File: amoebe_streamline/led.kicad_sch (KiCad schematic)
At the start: 1 part

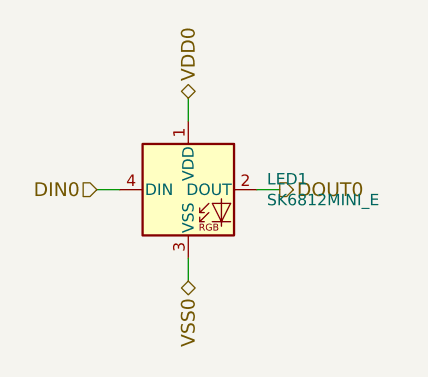
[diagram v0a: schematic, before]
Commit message: Finished schematic and routed traces
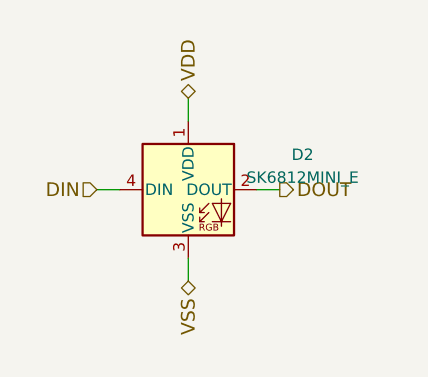
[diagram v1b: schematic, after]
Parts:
- removed LED1: SK6812MINI_E, amoeba-modules:LED_SK6812MINI_E_PLCC4_3.2x2.8mm_Shine_Through, symbol amoeba-king-rescue:SK6812MINI_E-amoeba-royale-rescue
- added D2: SK6812MINI_E, CustomFootprints:SK6812-MINI-E, symbol Amoebe_streamline:SK6812MINI_E
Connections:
- new net DIN: D2.4 (DIN)
- new net DOUT: D2.2 (DOUT)
- new net VDD: D2.1 (VDD)
- new net VSS: D2.3 (VSS)
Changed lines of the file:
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@@
     (stroke (width 0) (type default))
   )
-  (hierarchical_label "DOUT0" (shape output) (at 144.78 88.9 0) (fields_autoplaced)
+  (hierarchical_label "DOUT" (shape output) (at 144.78 88.9 0) (fields_autoplaced)
     (effects (font (size 1.524 1.524)) (justify left))
   )
-  (hierarchical_label "VSS0" (shape bidirectional) (at 134.62 99.06 270) (fields_autoplaced)
+  (hierarchical_label "VSS" (shape bidirectional) (at 134.62 99.06 270) (fields_autoplaced)
     (effects (font (size 1.524 1.524)) (justify right))
   )
-  (hierarchical_label "DIN0" (shape input) (at 124.46 88.9 180) (fields_autoplaced)
+  (hierarchical_label "DIN" (shape input) (at 124.46 88.9 180) (fields_autoplaced)
     (effects (font (size 1.524 1.524)) (justify right))
   )
-  (hierarchical_label "VDD0" (shape bidirectional) (at 134.62 78.74 90) (fields_autoplaced)
+  (hierarchical_label "VDD" (shape bidirectional) (at 134.62 78.74 90) (fields_autoplaced)
     (effects (font (size 1.524 1.524)) (justify left))
   )
-  (symbol (lib_id "amoeba-king-rescue:SK6812MINI_E-amoeba-royale-rescue") (at 134.62 88.9 0) (unit 1)
-    (in_bom yes) (on_board yes) (dnp no)
-    (property "Reference" "LED1" (at 143.3576 87.7316 0)
-      (effects (font (size 1.27 1.27)) (justify left))
+  (symbol (lib_id "Amoebe_streamline:SK6812MINI_E") (at 134.62 88.9 0) (unit 1)
+    (in_bom yes) (on_board yes) (dnp no) (fields_autoplaced)
+    (property "Reference" "D2" (at 147.32 85.0139 0)
+      (effects (font (size 1.27 1.27)))
     )
-    (property "Value" "SK6812MINI_E" (at 143.3576 90.043 0)
-      (effects (font (size 1.27 1.27)) (justify left))
+    (property "Value" "SK6812MINI_E" (at 147.32 87.5539 0)
+      (effects (font (size 1.27 1.27)))
     )
-    (property "Footprint" "amoeba-modules:LED_SK6812MINI_E_PLCC4_3.2x2.8mm_Shine_Through" (at 135.89 96.52 0)
+    (property "Footprint" "CustomFootprints:SK6812-MINI-E" (at 135.89 96.52 0)
       (effects (font (size 1.27 1.27)) (justify left top) hide)
     )
-    (property "Datasheet" "https://cdn-shop.adafruit.com/product-files/2686/SK6812MINI_REV.01-1-2.pdf" (at 137.16 98.425 0)
+    (property "Datasheet" "" (at 137.16 98.425 0)
       (effects (font (size 1.27 1.27)) (justify left top) hide)
     )
@@
     (pin "4")
     (instances
-      (project "amoeba-king"
-        (path "/75875c2f-4bf0-4a86-af0a-6af4e2048374/00000000-0000-0000-0000-000055d92fdb/00000000-0000-0000-0000-000055dbae59"
-          (reference "LED1") (unit 1)
+      (project "amoebe_streamline"
+        (path "/f7434787-4d52-45e0-bcf8-72783deb577d/49b013cb-3077-41ab-9637-70b1ae0af3e3/8b16eeb3-c182-4930-89bd-addfe26918e9"
+          (reference "D2") (unit 1)
         )
       )
-      (project "amoebe_streamline"
-        (path "/f7434787-4d52-45e0-bcf8-72783deb577d/49b013cb-3077-41ab-9637-70b1ae0af3e3/8b16eeb3-c182-4930-89bd-addfe26918e9"
-          (reference "LED1") (unit 1)
-        )
-      )
